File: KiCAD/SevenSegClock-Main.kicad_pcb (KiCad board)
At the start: 2 copper layers, 129.5 x 182.9 mm, 43 parts, among them J1101 Output, J1102 Output, J201 Input, J202 Output, U1101 AZ1117-5.0, U201 AZ1117-5.0

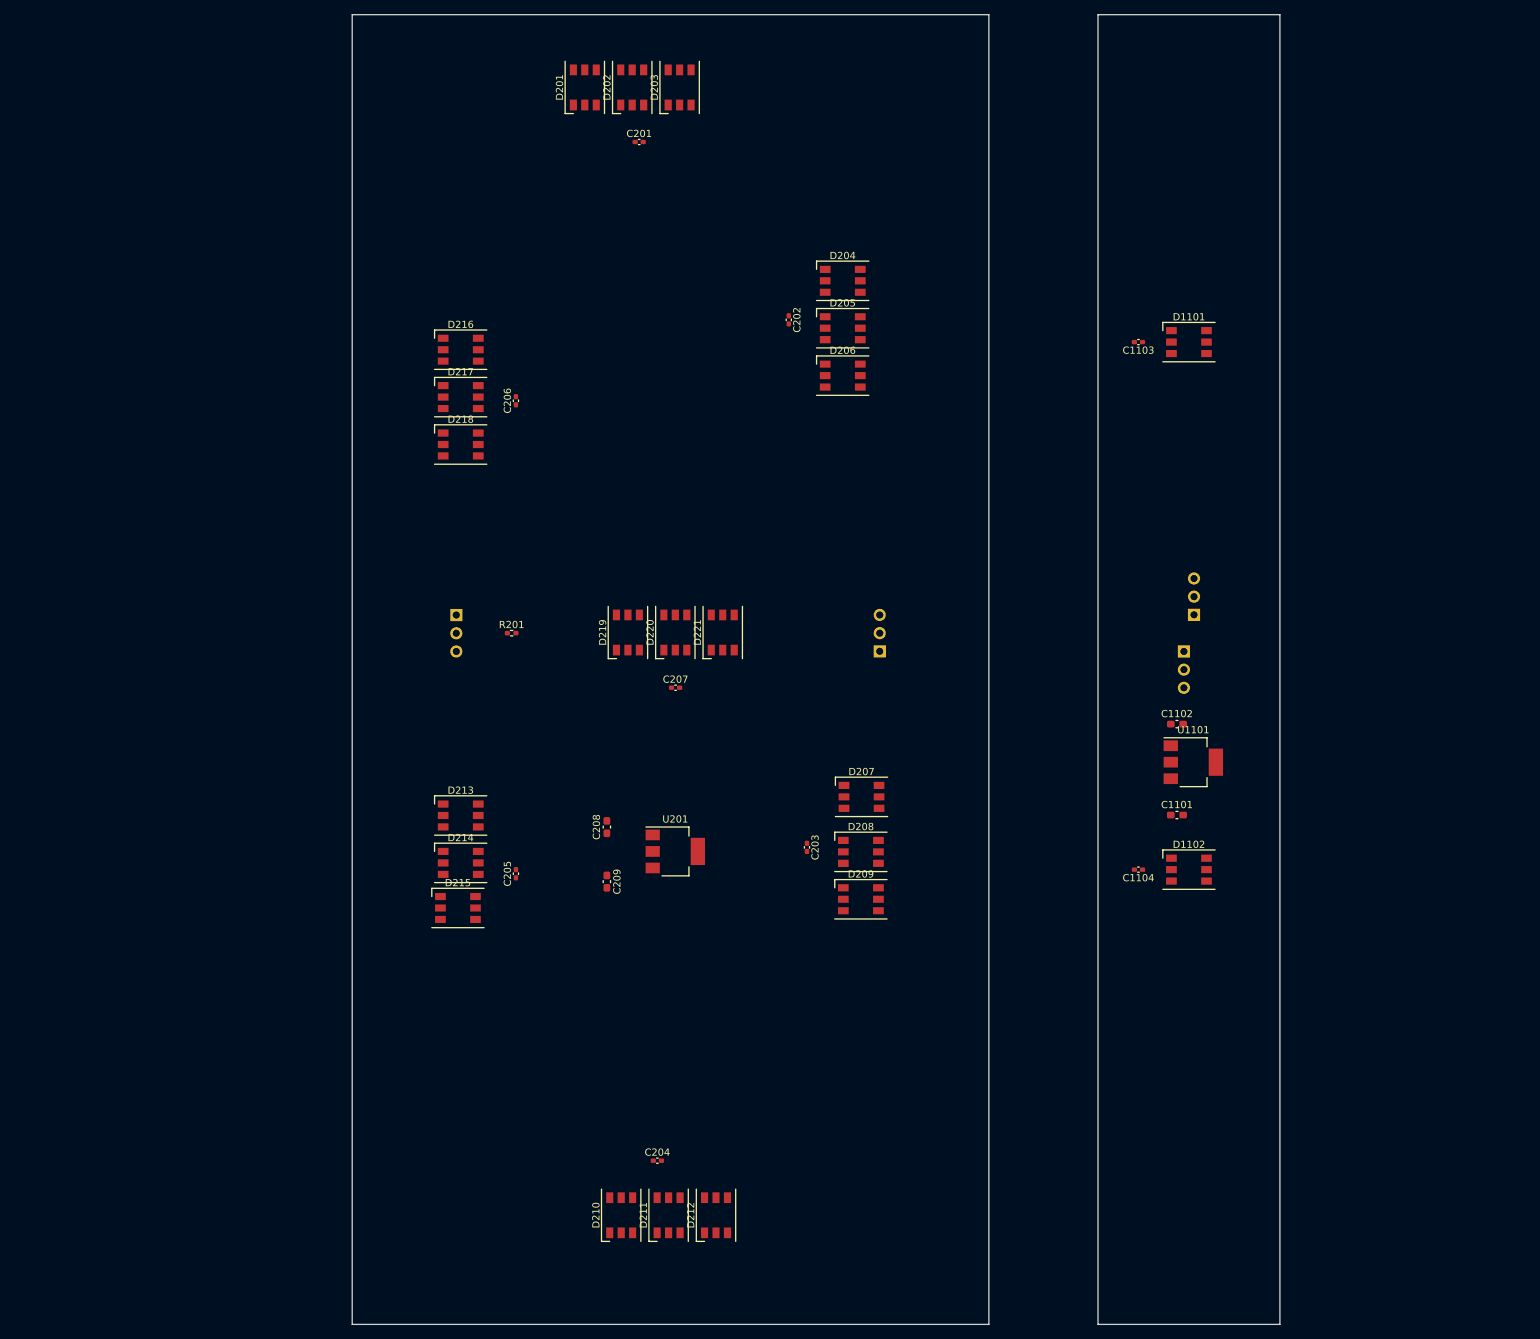
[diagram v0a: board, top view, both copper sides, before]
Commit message: Initial PCB layout for 7-seg digits
I realize now that the PCB for the digits needs to be slanted, otherwise the colon pcb won't fit next to it, grumble
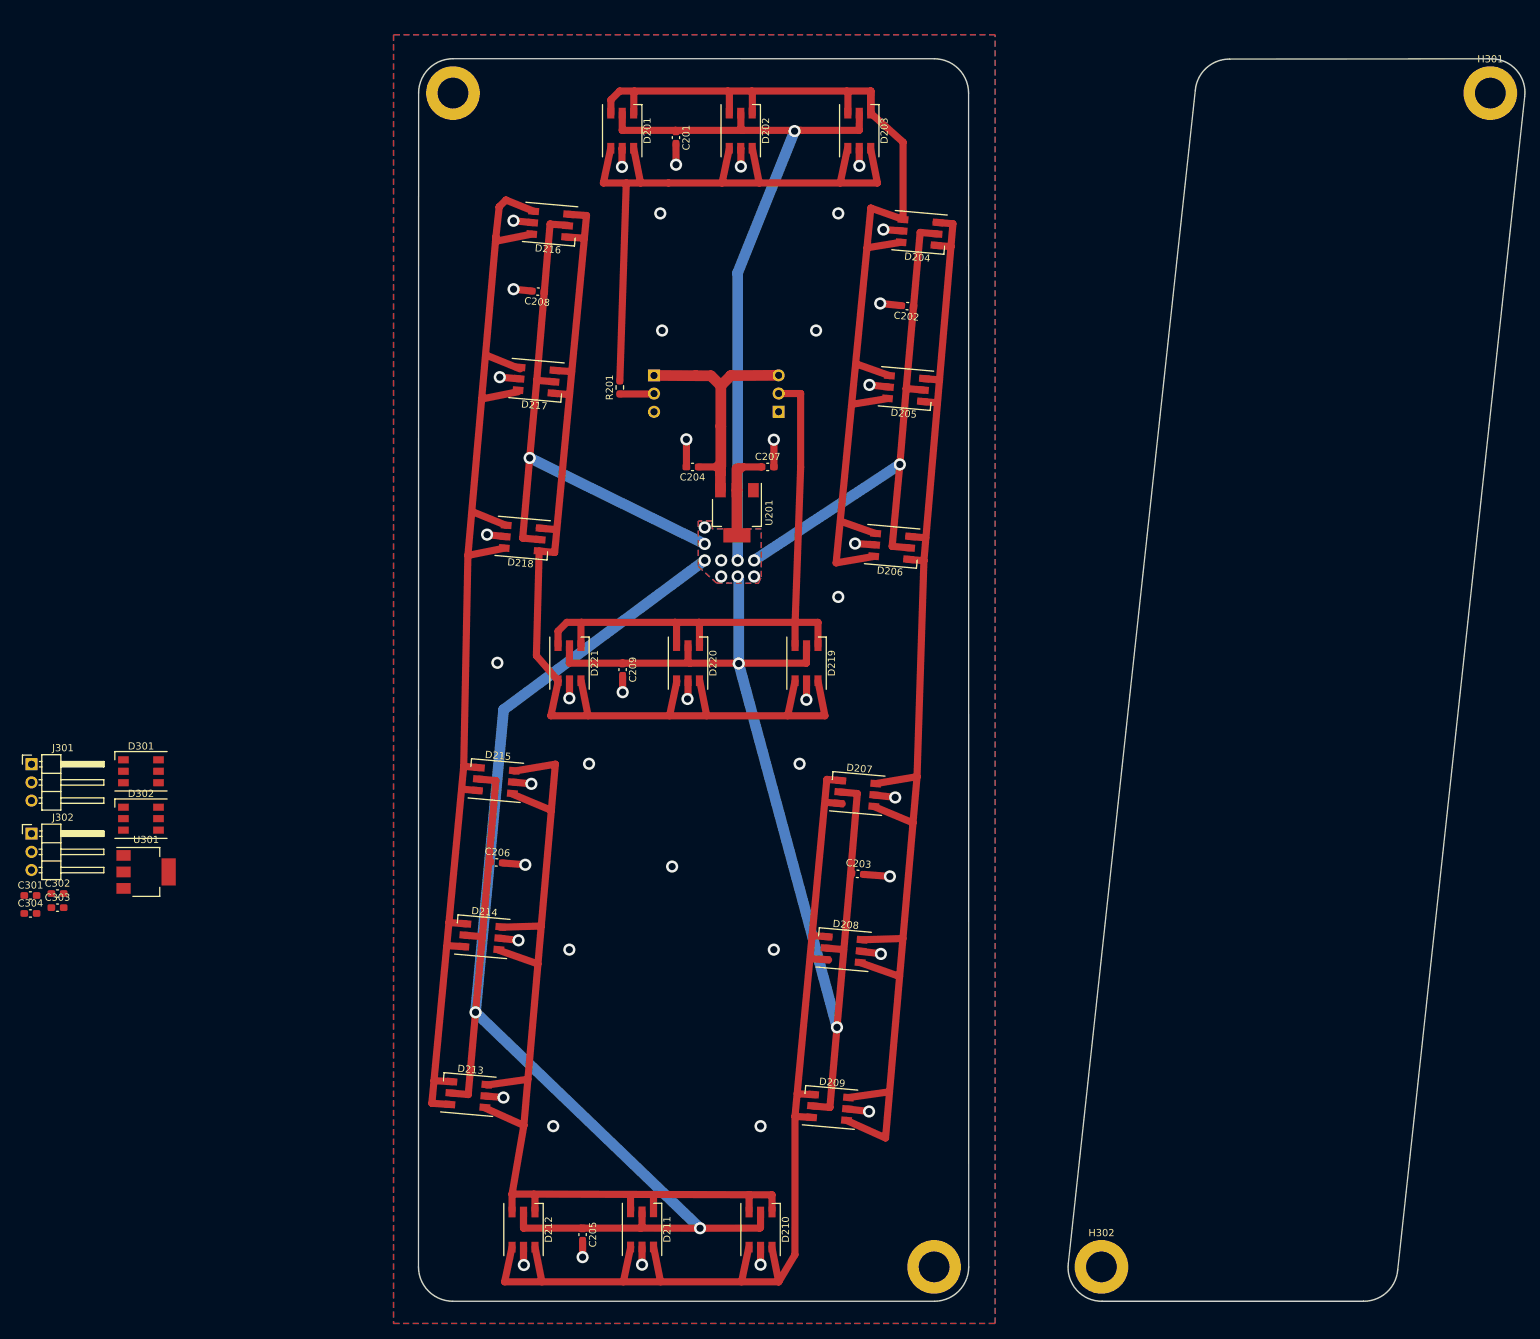
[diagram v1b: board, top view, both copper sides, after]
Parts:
- removed C1101, C1102: 10uF, Capacitor_SMD:C_0603_1608Metric_Pad1.08x0.95mm_HandSolder
- removed C1103, C1104: 1uF, Capacitor_SMD:C_0402_1005Metric_Pad0.74x0.62mm_HandSolder
- removed D1101, D1102: WS2813B, LED_SMD:LED_WS2812_PLCC6_5.0x5.0mm_P1.6mm
- removed J1101, J1102: Output, Connector_PinHeader_2.54mm:PinHeader_1x03_P2.54mm_Horizontal
- removed U1101: AZ1117-5.0, Package_TO_SOT_SMD:SOT-223-3_TabPin2
- added C301: 10uF, Capacitor_SMD:C_0603_1608Metric_Pad1.08x0.95mm_HandSolder, F.Cu at (-27.1, 135.7)
- added C302: 1uF, Capacitor_SMD:C_0603_1608Metric_Pad1.08x0.95mm_HandSolder, F.Cu at (-23.4, 135.4)
- added C303: 1uF, Capacitor_SMD:C_0603_1608Metric_Pad1.08x0.95mm_HandSolder, F.Cu at (-23.4, 137.4)
- added C304: 10uF, Capacitor_SMD:C_0603_1608Metric_Pad1.08x0.95mm_HandSolder, F.Cu at (-27.1, 138.2)
- added D301: WS2813B, LED_SMD:LED_WS2812_PLCC6_5.0x5.0mm_P1.6mm, F.Cu at (-11.7, 118.3)
- added D302: WS2813B, LED_SMD:LED_WS2812_PLCC6_5.0x5.0mm_P1.6mm, F.Cu at (-11.7, 125.0)
- added H201: M4, MountingHole:MountingHole_4.3mm_M4_DIN965_Pad, F.Cu at (31.9, 23.6)
- added H202: M4, MountingHole:MountingHole_4.3mm_M4_DIN965_Pad, F.Cu at (99.0, 187.5)
- added H301: M4, MountingHole:MountingHole_4.3mm_M4_DIN965_Pad, F.Cu at (176.7, 23.6)
- added H302: M4, MountingHole:MountingHole_4.3mm_M4_DIN965_Pad, F.Cu at (122.4, 187.5)
- added J301: Output, Connector_PinHeader_2.54mm:PinHeader_1x03_P2.54mm_Horizontal, F.Cu at (-27.0, 117.4)
- added J302: Output, Connector_PinHeader_2.54mm:PinHeader_1x03_P2.54mm_Horizontal, F.Cu at (-27.0, 127.1)
- added U301: AZ1117-5.0, Package_TO_SOT_SMD:SOT-223-3_TabPin2, F.Cu at (-11.0, 132.4)
- C201, C202, C203, C205, C206: footprint Capacitor_SMD:C_0402_1005Metric_Pad0.74x0.62mm_HandSolder -> Capacitor_SMD:C_0603_1608Metric_Pad1.08x0.95mm_HandSolder
- C204, C207: value 1uF -> 10uF; footprint Capacitor_SMD:C_0402_1005Metric_Pad0.74x0.62mm_HandSolder -> Capacitor_SMD:C_0603_1608Metric_Pad1.08x0.95mm_HandSolder
- C208, C209: value 10uF -> 1uF
- R201: footprint Resistor_SMD:R_0402_1005Metric_Pad0.72x0.64mm_HandSolder -> Resistor_SMD:R_0603_1608Metric_Pad0.98x0.95mm_HandSolder
- moved C204 97.0 mm to (65.3, 75.8), turned to 180 degrees
- moved C208 75.4 mm to (43.7, 51.4), turned to 175 degrees
- moved C206 64.5 mm to (37.9, 131.1), turned to -5 degrees
- moved C205 51.2 mm to (50.0, 183.0), turned to -90 degrees
- moved U201 48.1 mm to (71.5, 82.2), turned to -90 degrees
- moved J201 43.4 mm to (59.9, 63.1)
- moved D213 39.0 mm to (34.0, 163.5), turned to -5 degrees
- moved R201 37.5 mm to (55.1, 64.8), turned to 90 degrees
- moved J202 36.3 mm to (77.3, 68.1)
- moved C207 33.4 mm to (75.8, 75.8)
- moved C209 29.7 mm to (55.5, 104.2)
- moved D209 29.4 mm to (84.5, 165.3), turned to -5 degrees
- moved D212 27.0 mm to (41.7, 182.3), turned to -90 degrees
- moved D203 25.8 mm to (88.6, 28.9), turned to -90 degrees
- moved D219 25.3 mm to (81.2, 103.2), turned to -90 degrees
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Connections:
- net /Day 100s/A-B renamed /Seven Segment Digit/A-B
- net /Day 100s/B-C renamed /Seven Segment Digit/B-C
- net /Day 100s/DATA_IN renamed /Seven Segment Digit/DATA_IN
- net /Day 100s/DATA_OUT renamed /Seven Segment Digit/DATA_OUT
- C201 pad 1: /Day 100s/V5_0 -> /Seven Segment Digit/V5_0
- C201 pad 2: /Day 100s/GND -> /Seven Segment Digit/GND
- C202 pad 1: /Day 100s/V5_0 -> /Seven Segment Digit/V5_0
- C202 pad 2: /Day 100s/GND -> /Seven Segment Digit/GND
- C203 pad 1: /Day 100s/V5_0 -> /Seven Segment Digit/V5_0
- C203 pad 2: /Day 100s/GND -> /Seven Segment Digit/GND
- C204 pad 1: /Day 100s/V5_0 -> /Seven Segment Digit/VIN_12V
- C204 pad 2: /Day 100s/GND -> /Seven Segment Digit/GND
- C205 pad 1: /Day 100s/V5_0 -> /Seven Segment Digit/V5_0
- C205 pad 2: /Day 100s/GND -> /Seven Segment Digit/GND
- C206 pad 1: /Day 100s/V5_0 -> /Seven Segment Digit/V5_0
- C206 pad 2: /Day 100s/GND -> /Seven Segment Digit/GND
- C207 pad 1: /Day 100s/V5_0 -> /Seven Segment Digit/V5_0
- C207 pad 2: /Day 100s/GND -> /Seven Segment Digit/GND
- C208 pad 1: /Day 100s/V5_0 -> /Seven Segment Digit/V5_0
- C208 pad 2: /Day 100s/GND -> /Seven Segment Digit/GND
- C209 pad 1: /Day 100s/VIN_12V -> /Seven Segment Digit/V5_0
- C209 pad 2: /Day 100s/GND -> /Seven Segment Digit/GND
- D201 pad 2: /Day 100s/V5_0 -> /Seven Segment Digit/V5_0
- D201 pad 5: /Day 100s/GND -> /Seven Segment Digit/GND
- D202 pad 2: /Day 100s/V5_0 -> /Seven Segment Digit/V5_0
- D202 pad 5: /Day 100s/GND -> /Seven Segment Digit/GND
- D203 pad 2: /Day 100s/V5_0 -> /Seven Segment Digit/V5_0
- D203 pad 5: /Day 100s/GND -> /Seven Segment Digit/GND
- D204 pad 2: /Day 100s/V5_0 -> /Seven Segment Digit/V5_0
- D204 pad 5: /Day 100s/GND -> /Seven Segment Digit/GND
- D205 pad 2: /Day 100s/V5_0 -> /Seven Segment Digit/V5_0
- D205 pad 5: /Day 100s/GND -> /Seven Segment Digit/GND
- D206 pad 2: /Day 100s/V5_0 -> /Seven Segment Digit/V5_0
- D206 pad 5: /Day 100s/GND -> /Seven Segment Digit/GND
- D207 pad 1: /Day 100s/C-D -> /Seven Segment Digit/C-D
- D207 pad 2: /Day 100s/V5_0 -> /Seven Segment Digit/V5_0
- D207 pad 3: /Day 100s/C-D -> /Seven Segment Digit/C-D
- D207 pad 5: /Day 100s/GND -> /Seven Segment Digit/GND
- D208 pad 1: /Day 100s/C-D -> /Seven Segment Digit/C-D
- D208 pad 2: /Day 100s/V5_0 -> /Seven Segment Digit/V5_0
- D208 pad 3: /Day 100s/C-D -> /Seven Segment Digit/C-D
- D208 pad 5: /Day 100s/GND -> /Seven Segment Digit/GND
- D209 pad 1: /Day 100s/C-D -> /Seven Segment Digit/C-D
- D209 pad 2: /Day 100s/V5_0 -> /Seven Segment Digit/V5_0
- D209 pad 3: /Day 100s/C-D -> /Seven Segment Digit/C-D
- D209 pad 5: /Day 100s/GND -> /Seven Segment Digit/GND
- D210 pad 1: /Day 100s/D-E -> /Seven Segment Digit/D-E
- D210 pad 2: /Day 100s/V5_0 -> /Seven Segment Digit/V5_0
- D210 pad 3: /Day 100s/D-E -> /Seven Segment Digit/D-E
- D210 pad 4: /Day 100s/C-D -> /Seven Segment Digit/C-D
- D210 pad 5: /Day 100s/GND -> /Seven Segment Digit/GND
- D210 pad 6: /Day 100s/C-D -> /Seven Segment Digit/C-D
- D211 pad 1: /Day 100s/E-F -> /Seven Segment Digit/D-E
- D211 pad 2: /Day 100s/V5_0 -> /Seven Segment Digit/V5_0
- D211 pad 3: /Day 100s/E-F -> /Seven Segment Digit/D-E
- D211 pad 4: /Day 100s/D-E -> /Seven Segment Digit/C-D
- D211 pad 5: /Day 100s/GND -> /Seven Segment Digit/GND
- D211 pad 6: /Day 100s/D-E -> /Seven Segment Digit/C-D
- D212 pad 1: /Day 100s/F-G -> /Seven Segment Digit/D-E
- D212 pad 2: /Day 100s/V5_0 -> /Seven Segment Digit/V5_0
- D212 pad 3: /Day 100s/F-G -> /Seven Segment Digit/D-E
- D212 pad 4: /Day 100s/E-F -> /Seven Segment Digit/C-D
- D212 pad 5: /Day 100s/GND -> /Seven Segment Digit/GND
- D212 pad 6: /Day 100s/E-F -> /Seven Segment Digit/C-D
- D213 pad 1: /Day 100s/D-E -> /Seven Segment Digit/E-F
- D213 pad 2: /Day 100s/V5_0 -> /Seven Segment Digit/V5_0
- D213 pad 3: /Day 100s/D-E -> /Seven Segment Digit/E-F
- D213 pad 4: /Day 100s/C-D -> /Seven Segment Digit/D-E
- D213 pad 5: /Day 100s/GND -> /Seven Segment Digit/GND
- D213 pad 6: /Day 100s/C-D -> /Seven Segment Digit/D-E
- D214 pad 1: /Day 100s/E-F -> /Seven Segment Digit/E-F
- D214 pad 2: /Day 100s/V5_0 -> /Seven Segment Digit/V5_0
- D214 pad 3: /Day 100s/E-F -> /Seven Segment Digit/E-F
- D214 pad 4: /Day 100s/D-E -> /Seven Segment Digit/D-E
- D214 pad 5: /Day 100s/GND -> /Seven Segment Digit/GND
- D214 pad 6: /Day 100s/D-E -> /Seven Segment Digit/D-E
- D215 pad 1: /Day 100s/F-G -> /Seven Segment Digit/E-F
- D215 pad 2: /Day 100s/V5_0 -> /Seven Segment Digit/V5_0
- D215 pad 3: /Day 100s/F-G -> /Seven Segment Digit/E-F
- D215 pad 4: /Day 100s/E-F -> /Seven Segment Digit/D-E
- D215 pad 5: /Day 100s/GND -> /Seven Segment Digit/GND
- D215 pad 6: /Day 100s/E-F -> /Seven Segment Digit/D-E
- D216 pad 1: /Day 100s/D-E -> /Seven Segment Digit/F-G
- D216 pad 2: /Day 100s/V5_0 -> /Seven Segment Digit/V5_0
- D216 pad 3: /Day 100s/D-E -> /Seven Segment Digit/F-G
- D216 pad 4: /Day 100s/C-D -> /Seven Segment Digit/E-F
- D216 pad 5: /Day 100s/GND -> /Seven Segment Digit/GND
- D216 pad 6: /Day 100s/C-D -> /Seven Segment Digit/E-F
- D217 pad 1: /Day 100s/E-F -> /Seven Segment Digit/F-G
- D217 pad 2: /Day 100s/V5_0 -> /Seven Segment Digit/V5_0
- D217 pad 3: /Day 100s/E-F -> /Seven Segment Digit/F-G
- D217 pad 4: /Day 100s/D-E -> /Seven Segment Digit/E-F
- D217 pad 5: /Day 100s/GND -> /Seven Segment Digit/GND
- D217 pad 6: /Day 100s/D-E -> /Seven Segment Digit/E-F
- D218 pad 1: /Day 100s/F-G -> /Seven Segment Digit/F-G
- D218 pad 2: /Day 100s/V5_0 -> /Seven Segment Digit/V5_0
- D218 pad 3: /Day 100s/F-G -> /Seven Segment Digit/F-G
- D218 pad 4: /Day 100s/E-F -> /Seven Segment Digit/E-F
- D218 pad 5: /Day 100s/GND -> /Seven Segment Digit/GND
- D218 pad 6: /Day 100s/E-F -> /Seven Segment Digit/E-F
- D219 pad 2: /Day 100s/V5_0 -> /Seven Segment Digit/V5_0
- D219 pad 4: /Day 100s/F-G -> /Seven Segment Digit/F-G
- D219 pad 5: /Day 100s/GND -> /Seven Segment Digit/GND
- D219 pad 6: /Day 100s/F-G -> /Seven Segment Digit/F-G
- D220 pad 2: /Day 100s/V5_0 -> /Seven Segment Digit/V5_0
- D220 pad 4: /Day 100s/F-G -> /Seven Segment Digit/F-G
- D220 pad 5: /Day 100s/GND -> /Seven Segment Digit/GND
- D220 pad 6: /Day 100s/F-G -> /Seven Segment Digit/F-G
- D221 pad 2: /Day 100s/V5_0 -> /Seven Segment Digit/V5_0
- D221 pad 4: /Day 100s/F-G -> /Seven Segment Digit/F-G
- D221 pad 5: /Day 100s/GND -> /Seven Segment Digit/GND
- D221 pad 6: /Day 100s/F-G -> /Seven Segment Digit/F-G
- J201 pad 1: /Day 100s/VIN_12V -> /Seven Segment Digit/VIN_12V
- J201 pad 3: /Day 100s/GND -> /Seven Segment Digit/GND
- J202 pad 1: /Day 100s/VIN_12V -> /Seven Segment Digit/GND
- J202 pad 3: /Day 100s/GND -> /Seven Segment Digit/VIN_12V
- U201 pad 1: /Day 100s/GND -> /Seven Segment Digit/GND
- U201 pad 2: /Day 100s/V5_0 -> /Seven Segment Digit/V5_0
- U201 pad 3: /Day 100s/VIN_12V -> /Seven Segment Digit/VIN_12V
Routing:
- net /Seven Segment Digit/V5_0: track 0.00 -> 640.6 mm, vias 0 -> 16
- net /Seven Segment Digit/B-C: track 0.00 -> 177.3 mm
- net /Seven Segment Digit/E-F: track 0.00 -> 171.1 mm
- net /Seven Segment Digit/A-B: track 0.00 -> 153.5 mm
- net /Seven Segment Digit/C-D: track 0.00 -> 153.4 mm
- net /Seven Segment Digit/F-G: track 0.00 -> 148.9 mm
- net /Seven Segment Digit/D-E: track 0.00 -> 145.1 mm
- net /Seven Segment Digit/DATA_IN: track 0.00 -> 95.6 mm
- net /Seven Segment Digit/DATA_OUT: track 0.00 -> 90.5 mm
- net /Seven Segment Digit/GND: track 0.00 -> 83.1 mm, vias 0 -> 43
- net /Seven Segment Digit/VIN_12V: track 0.00 -> 38.7 mm
- net Net-(J201-Pin_2): track 0.00 -> 4.79 mm
- added copper zone on B.Cu, net /Seven Segment Digit/GND
- added copper zone on F.Cu, net /Seven Segment Digit/GND
- added copper zone on B.Cu, net /Seven Segment Digit/V5_0
- added copper zone on F.Cu, net /Seven Segment Digit/V5_0
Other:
- board size 129.5 x 182.9 mm -> 154.5 x 173.5 mm
